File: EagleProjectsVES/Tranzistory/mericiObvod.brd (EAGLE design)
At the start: 160 x 100 mm, 73 parts, among them IC1 TLC272P, IC2 TLC272P, IC3 NE555N, IC4 NE555N, IC5 TLC271P, K1 M3XXH, K2 M3XXH, K3 M3XXH, K4 M3XXH, Q1 BC557B, U12V SMKDSP_1,5/2

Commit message: Navrzena DPS pro mereni tranzistoru. Vyroba musi byt v Pragoboardu.
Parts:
- added R29, R30, R31, R32, R33, R34, R35, R36, R37, R38, R39, R40, R41, R42, R43, R46: 1R, rcl:R0805
- added R44, R45, R47, R48, R49, R50: 120R, rcl:R0805
- C1, C11, C12, C15, C2, C3, C4, C5, C6, C7, C8, C9: device rcl:C050-030X075 -> rcl:C0805K
- D3, D4: value 1N4148DO35-7 -> (none); device diode:DO35-7 -> semicon-smd-ipc:SOD80
- IC1, IC2: value TLC272P -> TLC272D; device linear:DIL08 -> linear:SO08
- IC3, IC4: value NE555N -> NE555D; device linear:DIL08 -> linear:SO08
- IC5: value TLC271P -> TLC271D; device linear:DIL08 -> linear:SO08
- R1, R10, R11, R12, R13, R14, R15, R16, R17, R18, R19, R2, R20, R22, R23, R25, R26, R27, R28, R3, R4, R5, R6, R7, R9: device rcl:0207/10 -> rcl:R0805
- R24: value 1R -> 120R; device rcl:0207/10 -> rcl:R0805
- R8: value (none) -> 120R; device rcl:0207/10 -> rcl:R0805
- moved R7 245.1 mm to (147.3, 47.3), turned to 270 degrees
- moved C14 237.4 mm to (143.5, 35.6), turned to 180 degrees
- moved R13 219.5 mm to (136.2, 69.5), turned to 270 degrees
- moved POT 216.6 mm to (123.2, 6.35), turned to 180 degrees
- moved R28 215.2 mm to (129.2, 59.7), turned to 180 degrees
- moved C11 207.6 mm to (132.4, 70.5), turned to 180 degrees
- moved C5 207.3 mm to (137.2, 66.0)
- moved R19 207.0 mm to (132.1, 47.3), turned to 270 degrees
- moved R22 204.8 mm to (106.7, 58.4), turned to 90 degrees
- moved KOLEKTOR 201.9 mm to (118.1, 77.5)
- moved R18 198.3 mm to (135.9, 47.3), turned to 270 degrees
- moved UCE2 193.0 mm to (143.5, 6.35), turned to 180 degrees
- moved R6 191.6 mm to (106.0, 48.9)
- moved R11 189.8 mm to (132.4, 77.5), turned to 180 degrees
- moved R17 189.7 mm to (139.7, 47.3), turned to 270 degrees
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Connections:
- new net N$48: K3.P, K3.P@, R3.2, R34.2, R35.2, R36.2, R37.2, R38.2, R39.2, R40.2, R41.2, R42.2, R43.2
- new net N$8: R16.2, R17.2, R18.2, R19.2, R29.2, R30.2, R31.2, R32.2, R33.2, R34.1, R35.1, R36.1, R37.1, R38.1, R39.1, R40.1, R41.1, R42.1, R43.1, R7.2
- net GND: now also K1.1, K3.1; no longer K1.2, K3.2
- net N$11: now also R29.1, R30.1, R31.1, R32.1, R33.1
- net N$12: now also R24.1, R44.1, R45.1, R47.2, R48.2, R49.2, R50.2, R8.1; no longer K3.P, K3.P@, R16.2, R17.2, R18.2, R19.2, R3.2, R7.2
- net N$13: now also R46.2; no longer R24.2
- net N$16: now also R46.1; no longer R24.1
- net N$17: now also R24.2, R44.2, R45.2
- net N$18: now also K1.2; no longer K1.1
- net N$21: now also K3.2; no longer K3.1
- net N$22: now also D3.2, D4.2; no longer D3.A, D4.A
- net N$32: now also R21.1; no longer R21.3
- net N$33: now also R21.3; no longer R21.1
- net VCC: now also D3.1, D4.1, R47.1, R48.1, R49.1, R50.1; no longer D3.C, D4.C, R8.1
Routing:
- net VCC: track 0.00 -> 379.4 mm, vias 0 -> 10
- net N$22: track 0.00 -> 125.5 mm
- net N$11: track 0.00 -> 102.5 mm
- net N$13: track 0.00 -> 95.1 mm, vias 0 -> 1
- net N$48: track 0.00 -> 58.7 mm, vias 0 -> 1
- net GND: track 0.00 -> 58.1 mm, vias 0 -> 15
- net N$10: track 0.00 -> 55.3 mm, vias 0 -> 1
- net N$18: track 0.00 -> 34.7 mm
- net N$21: track 0.00 -> 33.3 mm
- net N$2: track 0.00 -> 30.4 mm
- net N$4: track 0.00 -> 28.6 mm
- net N$15: track 0.00 -> 28.1 mm
- net N$3: track 0.00 -> 25.8 mm
- net N$20: track 0.00 -> 24.4 mm
- net N$33: track 0.00 -> 22.8 mm, vias 0 -> 1
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- added copper zone on layer 16, net GND
- added copper zone on layer 1, net N$12
- added copper zone on layer 1, net N$8

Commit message: Tranzistory predany k vyrobe
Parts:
- removed Q1: BC557B, transistor-pnp:TO92-EBC
- added D5: LL4148, semicon-smd-ipc:SOD80
- added H1, H2, H3, H4: MOUNT-PAD-ROUND3.2, holes:3,2-PAD
- added T3: BC557B, transistor-pnp:TO92-EBC
- C1, C2, C3: value (none) -> 470n
- C4, C5: value (none) -> 10u
- D3, D4: value (none) -> LL4148
- R1, R2: value 100k -> 1M
- R10, R11, R14, R15, R25, R26, R27, R28, R3, R5: value (none) -> 2k2
- R12: value (none) -> 47k
- R13: value (none) -> 100k
- R21: value (none) -> 25k
- R22, R23, R4, R6: value (none) -> 11k
- R9: value (none) -> 5k1
- moved R36 80.9 mm to (70.2, 17.8), turned to 180 degrees
- moved R7 77.9 mm to (75.2, 17.8), turned to 180 degrees
- moved R35 76.2 mm to (70.2, 21.6), turned to 180 degrees
- moved R16 72.9 mm to (75.2, 21.6), turned to 180 degrees
- moved R34 71.5 mm to (70.2, 25.4), turned to 180 degrees
- moved R17 68.1 mm to (75.2, 25.4), turned to 180 degrees
- moved R37 67.0 mm to (70.2, 29.2), turned to 180 degrees
- moved C14 64.1 mm to (81.3, 20.3), turned to 90 degrees
- moved R18 63.3 mm to (75.2, 29.2), turned to 180 degrees
- moved R39 62.6 mm to (70.2, 33.0), turned to 180 degrees
- moved LED2 62.3 mm to (50.8, 73.7), turned to 270 degrees
- moved R19 58.6 mm to (75.2, 33.0), turned to 180 degrees
- moved D2 58.4 mm to (44.5, 64.8)
- moved R38 58.4 mm to (70.2, 36.8), turned to 180 degrees
- moved R15 57.2 mm to (50.8, 78.7), turned to 270 degrees
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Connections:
- new net N$14: D5.2, POT.2
- net GND: now also H1.B3,2, H2.B3,2, H3.B3,2, H4.B3,2
- net N$15: now also D5.1, T3.B; no longer POT.2, Q1.B
- net N$16: now also T3.C; no longer Q1.C
- net N$17: now also T3.E; no longer Q1.E
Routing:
- net VCC: track 379.4 -> 406.2 mm, vias 10 -> 8
- net N$15: track 28.1 -> 9.26 mm
- net N$48: track 58.7 -> 74.0 mm
- net N$14: track 0.00 -> 13.2 mm
- net N$20: track 24.4 -> 30.3 mm
- net N$16: track 21.9 -> 18.1 mm
- net N$17: track 15.4 -> 17.7 mm
- net N$21: track 33.3 -> 31.1 mm
- net N$22: track 125.5 -> 127.3 mm
- net N$23: track 4.13 -> 2.54 mm
- net N$34: track 14.0 -> 12.4 mm
- net GND: track 58.1 -> 59.4 mm
- net N$13: track 95.1 -> 96.1 mm
- net N$10: track 55.3 -> 54.6 mm
- net N$33: track 22.8 -> 22.0 mm
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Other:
- board size 160 x 100 mm -> 95.2 x 84.8 mm

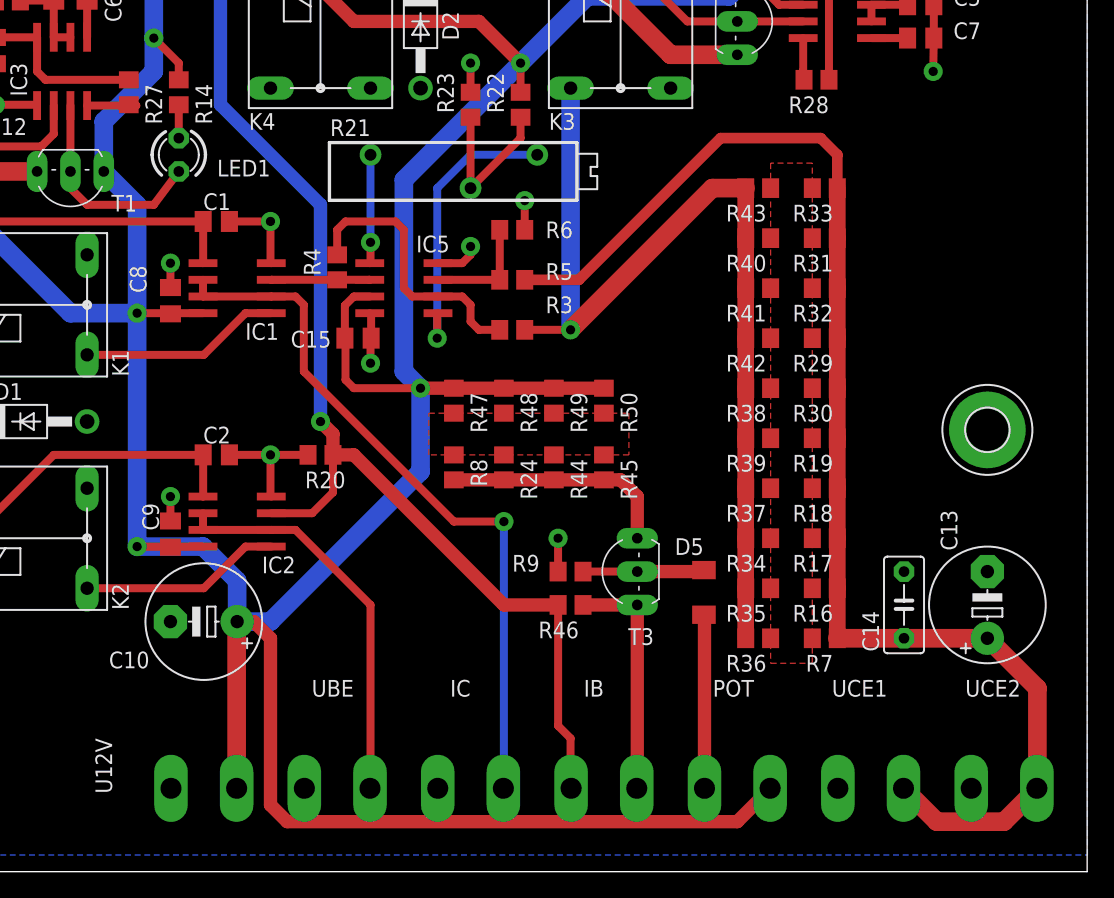
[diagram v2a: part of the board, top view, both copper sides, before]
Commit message: DPS Tranzistory: - opraveny chyby v desce, nyni by mela byt pouzitelna az do 30 V UCE
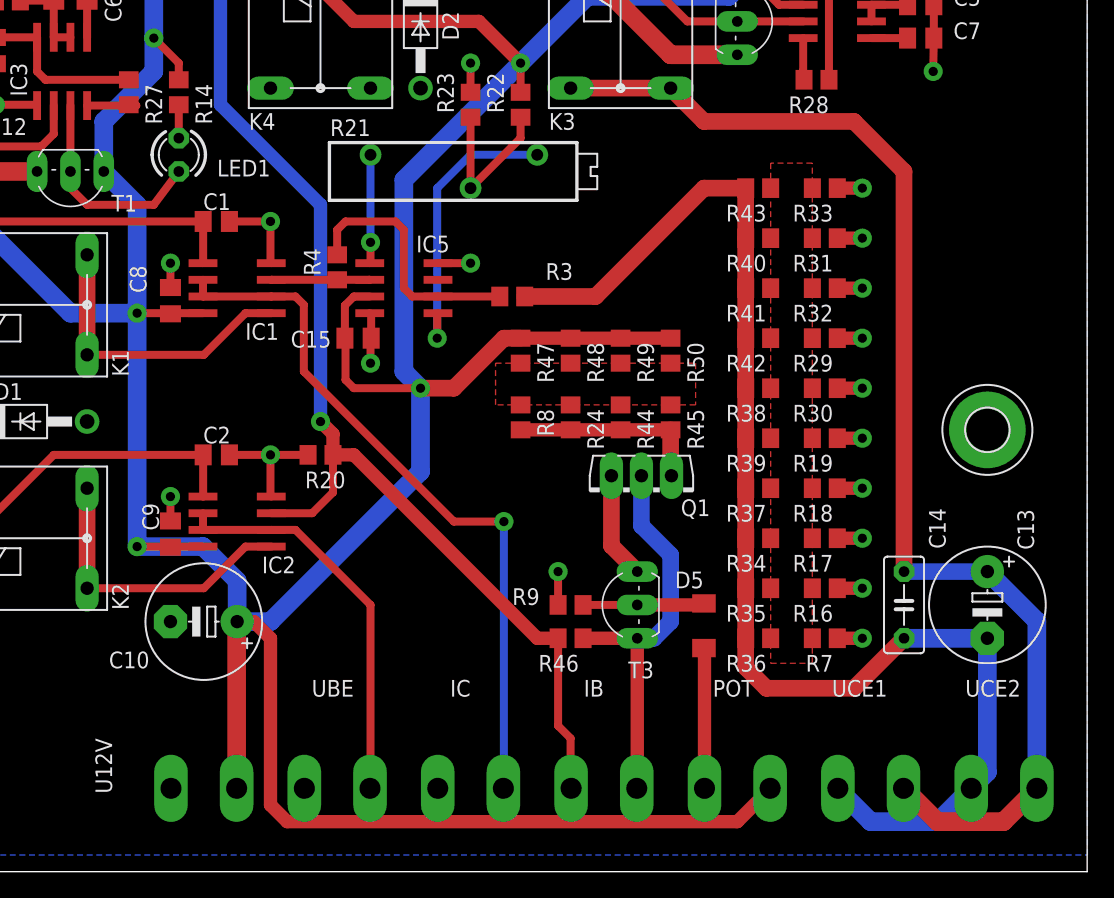
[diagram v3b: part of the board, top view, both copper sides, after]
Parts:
- removed R5: 2k2, rcl:R0805
- removed R6: 11k, rcl:R0805
- added Q1: BD140, transistor-power:TO126AV
- moved R24 6.35 mm to (55.9, 34.6)
- moved R48 6.35 mm to (55.9, 39.7)
- moved R44 6.35 mm to (59.7, 34.6)
- moved R45 6.35 mm to (63.5, 34.6)
- moved R47 6.35 mm to (52.1, 39.7)
- moved R49 6.35 mm to (59.7, 39.7)
- moved R50 6.35 mm to (63.5, 39.7)
- moved R8 6.35 mm to (52.1, 34.6)
- moved D5 2.54 mm to (66.0, 18.7)
- moved R3 2.54 mm to (51.4, 43.8)
- moved R46 2.54 mm to (55.9, 17.8)
- moved R9 2.54 mm to (55.9, 20.3)
- moved T3 2.54 mm to (59.7, 20.3)
- turned C13 to 270 degrees
- turned C14 to 270 degrees
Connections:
- removed net N$11: C13.+, C14.1, R16.1, R17.1, R18.1, R19.1, R29.1, R30.1, R31.1, R32.1, R33.1, R5.2, R7.1, UCE1.1, UCE2.1
- new net N$40: C13.+, C14.1, K3.P, K3.P@, UCE1.1, UCE2.1
- net GND: now also IC5.3, R16.1, R17.1, R18.1, R19.1, R29.1, R30.1, R31.1, R32.1, R33.1, R7.1; no longer C13.-, C14.2, R6.2, UCE1.2, UCE2.2
- net N$16: now also Q1.C
- net N$17: now also Q1.E; no longer T3.E
- net N$48: now also C13.-, C14.2, UCE1.2, UCE2.2; no longer K3.P, K3.P@
- net N$9: now also Q1.B, T3.E; no longer IC5.3, R5.1, R6.1
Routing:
- net N$11: track 102.4 -> 0.00 mm
- net N$40: track 0.00 -> 95.2 mm
- net N$48: track 74.0 -> 101.6 mm, vias 1 -> 0
- net GND: track 59.4 -> 75.3 mm, vias 15 -> 24
- net N$16: track 18.1 -> 30.7 mm
- net N$6: track 15.3 -> 23.0 mm
- net N$5: track 15.3 -> 23.0 mm
- net VCC: track 406.2 -> 412.9 mm
- net N$17: track 17.7 -> 15.0 mm
- net N$14: track 13.2 -> 10.7 mm
- net N$1: track 21.3 -> 19.5 mm
- net N$13: track 96.1 -> 94.6 mm
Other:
- board text added: "POZOR: 12 V zdroj musi byt galvanicky oddeleny od zdroje UCE"

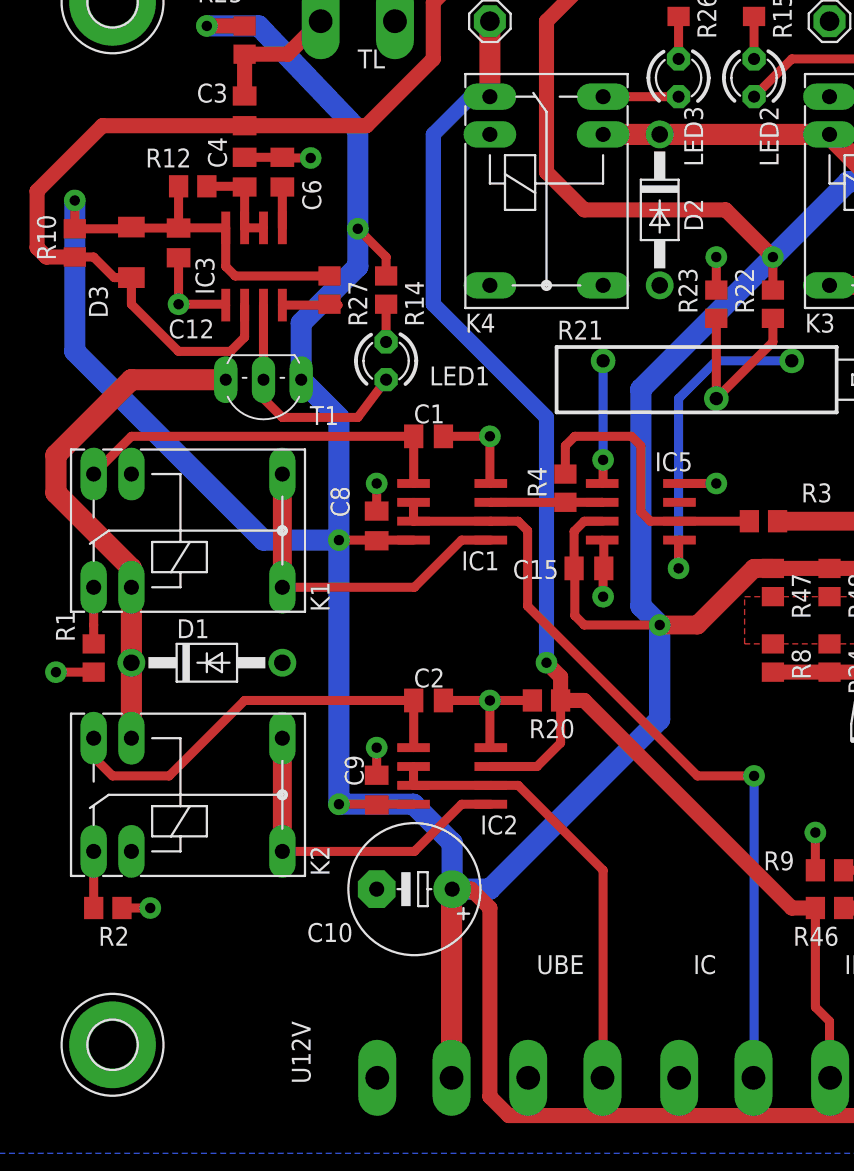
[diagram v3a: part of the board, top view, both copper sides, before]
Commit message: DPS Tranzisotry: - snizeno zesileni zpetne vazby - pridan odpor ke kondenzatoru sample-hold tak, aby vytvoril integracni clanek.
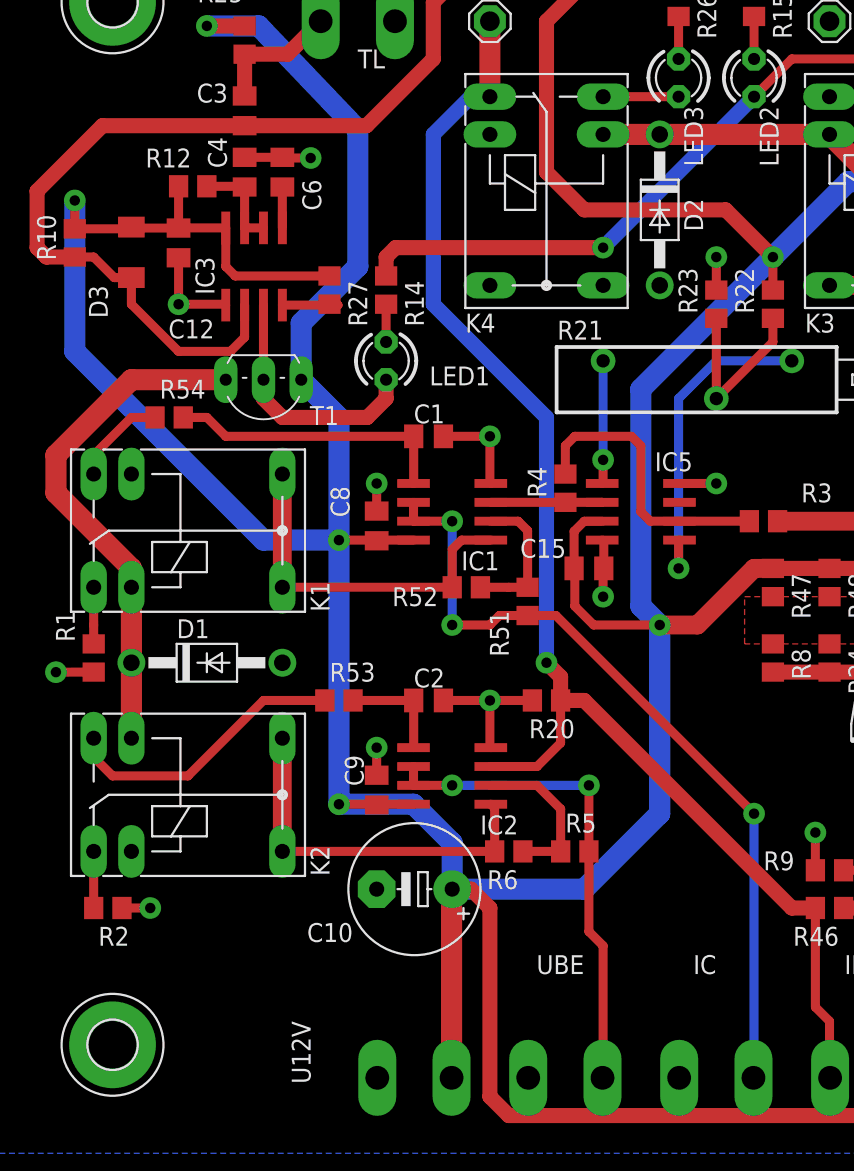
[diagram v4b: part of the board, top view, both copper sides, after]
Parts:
- added R5, R51: 1k, rcl:R0805
- added R52, R6: 100k, rcl:R0805
- added R53, R54: 100R, rcl:R0805
- R12: value 47k -> 82k
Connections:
- new net N$11: IC2.2, R5.1, R6.1
- new net N$39: IC1.2, R51.1, R52.1
- new net N$41: K1.S, R54.1
- new net N$42: K2.S, R53.1
- net N$10: now also R51.2; no longer IC1.2
- net N$2: now also R5.2; no longer IC2.2
- net N$20: now also R14.1
- net N$3: now also R54.2; no longer K1.S
- net N$4: now also R53.2; no longer K2.S
- net N$5: now also R6.2
- net N$6: now also R52.2
- net VCC: no longer R14.1
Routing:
- net N$20: track 30.3 -> 60.8 mm, vias 0 -> 1
- net N$4: track 28.6 -> 7.26 mm
- net N$42: track 0.00 -> 19.5 mm
- net N$11: track 0.00 -> 10.8 mm
- net N$39: track 0.00 -> 9.73 mm
- net N$3: track 25.8 -> 19.2 mm
- net N$41: track 0.00 -> 6.45 mm
- net N$2: track 30.4 -> 33.2 mm, vias 0 -> 2
- net N$5: track 23.0 -> 25.2 mm
- net N$6: track 23.0 -> 24.5 mm
- net VCC: track 412.9 -> 412.2 mm, vias 8 -> 7
- net N$19: track 16.3 -> 16.9 mm
- net N$10: track 54.6 -> 54.8 mm, vias 1 -> 3

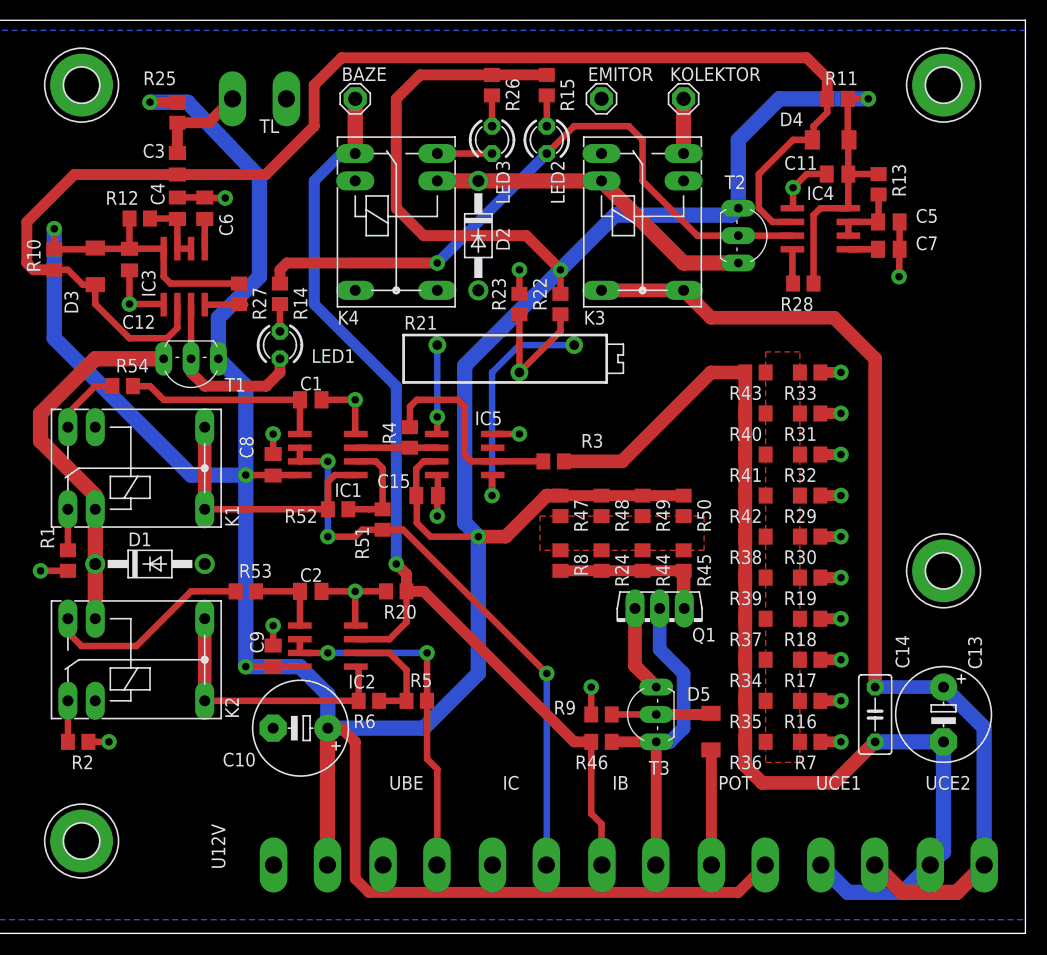
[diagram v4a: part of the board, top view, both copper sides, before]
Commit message: Eagle: - vybijec pro Papeze - tranzistory pred odeslanim do pragoboardu - navrh zdroju proudu
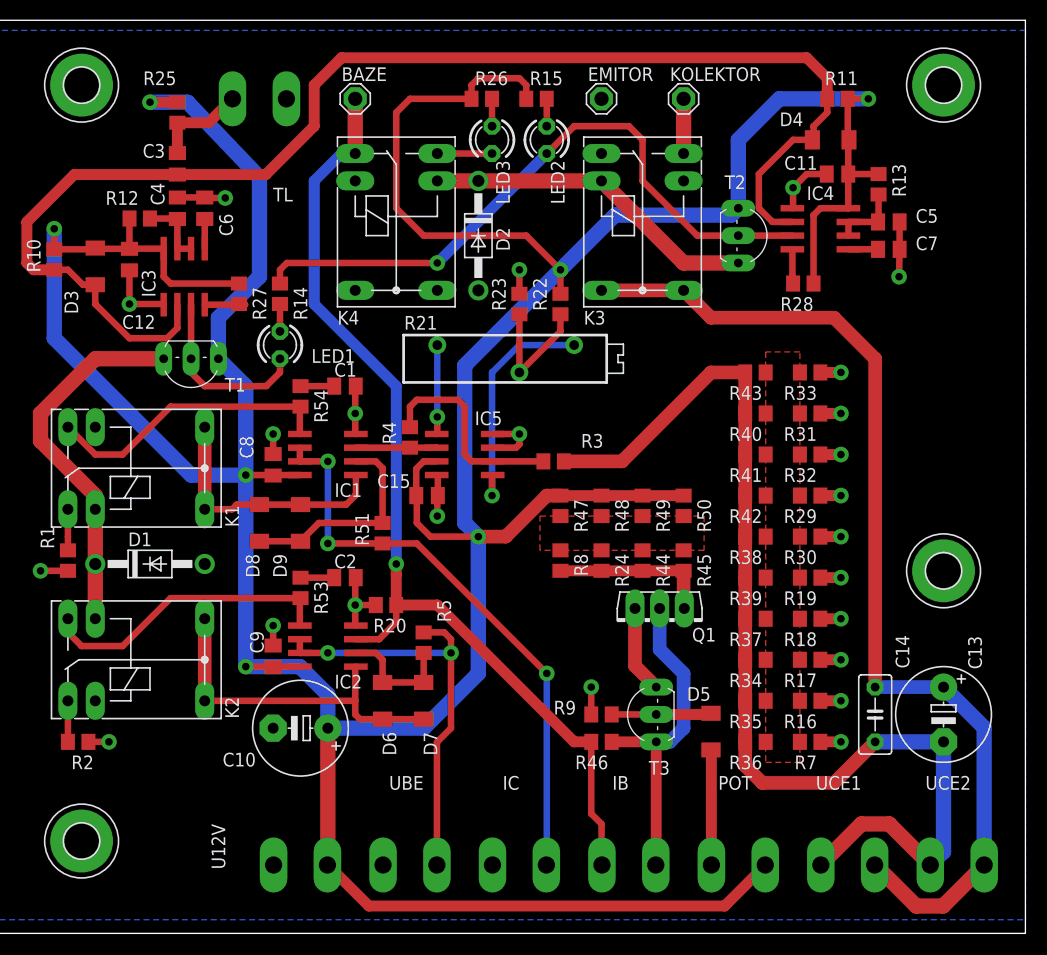
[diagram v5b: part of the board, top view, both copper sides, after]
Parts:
- removed R52, R6: 100k, rcl:R0805
- added D6, D7, D8, D9: LL4148, semicon-smd-ipc:SOD80
- C14: value 100n -> 470n
- T1, T2: value (none) -> BC547
- moved R54 16.5 mm to (27.9, 49.8), turned to 270 degrees
- moved R5 5.43 mm to (39.4, 27.0), turned to 90 degrees
- moved R53 5.09 mm to (27.9, 32.1), turned to 270 degrees
- moved C2 3.42 mm to (32.1, 33.0)
- moved C1 3.42 mm to (32.1, 50.8)
- moved R20 1.59 mm to (35.9, 30.5)
- moved R15 1.59 mm to (49.8, 77.5), turned to 0 degrees
- moved R26 1.59 mm to (44.8, 77.5), turned to 0 degrees
- moved R51 1.27 mm to (35.6, 37.1)
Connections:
- net N$11: now also D6.2, D7.1; no longer R6.1
- net N$3: now also R54.1; no longer IC1.5, R54.2
- net N$39: now also D8.2, D9.1; no longer R52.1
- net N$4: now also R53.1; no longer IC2.5, R53.2
- net N$41: now also IC1.5, R54.2; no longer R54.1
- net N$42: now also IC2.5, R53.2; no longer R53.1
- net N$5: now also D6.1, D7.2; no longer R6.2
- net N$6: now also D8.1, D9.2; no longer R52.2
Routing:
- net N$41: track 6.45 -> 27.0 mm
- net N$3: track 19.2 -> 3.13 mm
- net VCC: track 412.2 -> 400.1 mm
- net N$39: track 9.73 -> 20.0 mm
- net N$42: track 19.5 -> 27.8 mm
- net N$5: track 25.2 -> 32.6 mm
- net N$2: track 33.2 -> 39.6 mm
- net N$4: track 7.26 -> 3.13 mm
- net GND: track 75.3 -> 74.2 mm
- net N$48: track 101.6 -> 102.7 mm
- net N$40: track 95.2 -> 96.2 mm
- net N$13: track 94.6 -> 93.7 mm
- net N$11: track 10.8 -> 11.4 mm
